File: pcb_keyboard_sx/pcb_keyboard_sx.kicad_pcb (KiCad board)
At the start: 2 copper layers, 172.4 x 135.7 mm, 123 parts, among them SW1 BOOT button, U1 Pico, U2 TRRS

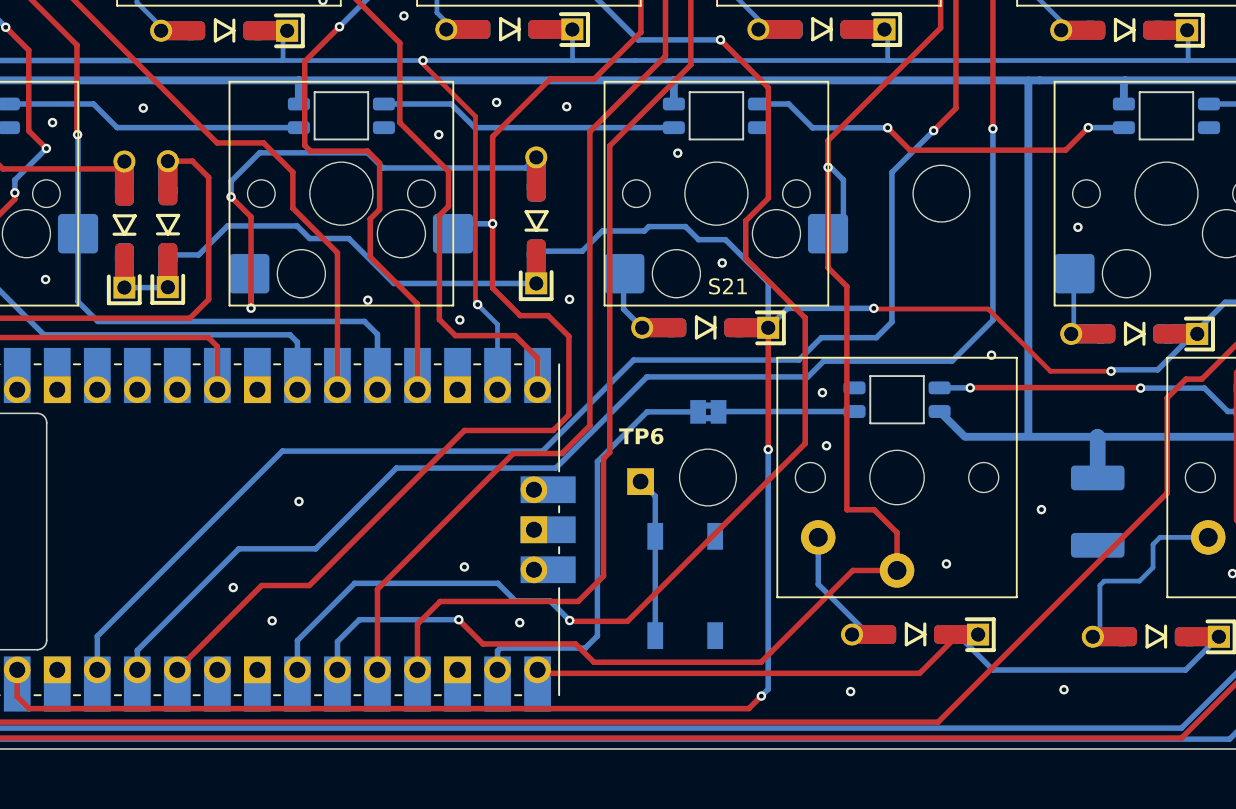
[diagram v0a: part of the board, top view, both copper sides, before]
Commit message: level shifter added also for sx part
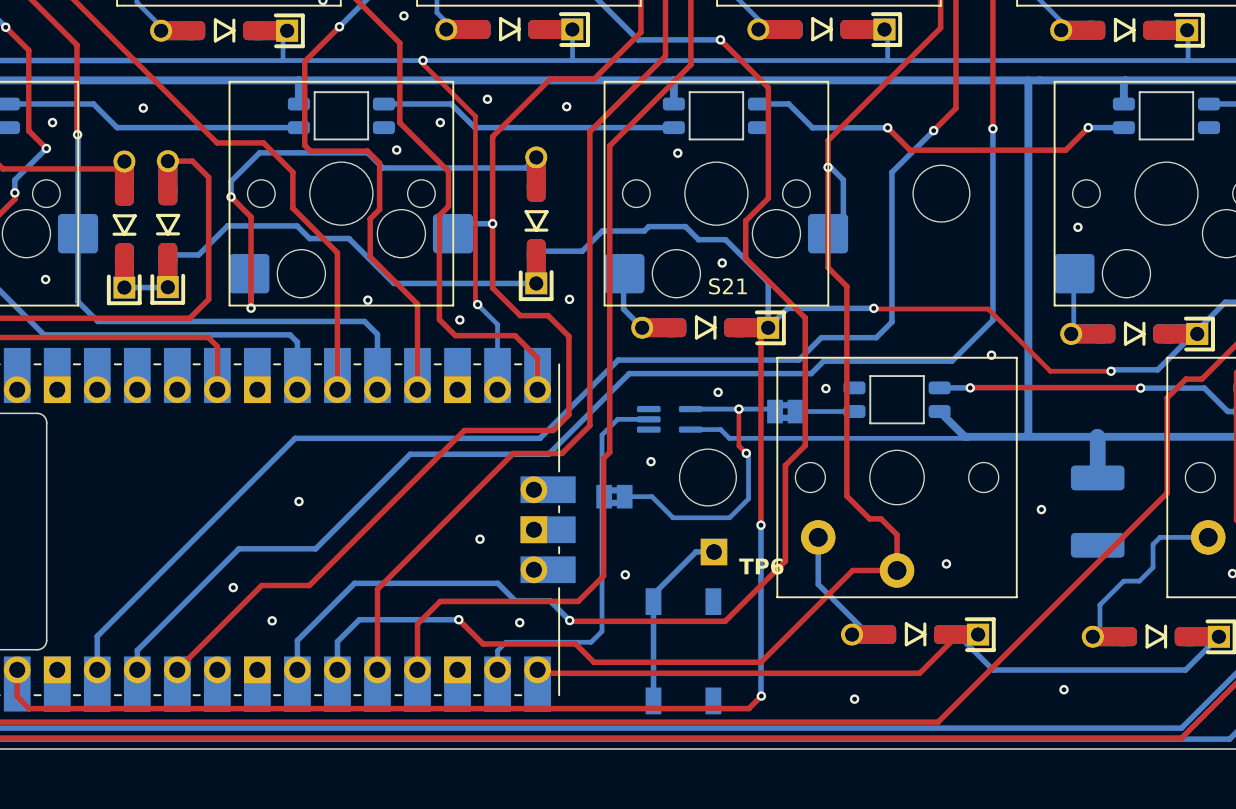
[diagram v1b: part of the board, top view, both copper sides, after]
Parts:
- added JP4: Jumper_2_Bridged, Jumper:SolderJumper-2_P1.3mm_Bridged2Bar_Pad1.0x1.5mm, B.Cu at (98.0, 142.4)
- added U3: 74LVC1G34, Package_TO_SOT_SMD:SOT-353_SC-70-5_Handsoldering, B.Cu at (101.5, 137.5)
- moved TP5 6.46 mm to (104.3, 145.9)
- moved JP3 4.88 mm to (108.9, 137.0)
- moved SW1 4.14 mm to (102.4, 152.2)
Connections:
- JP3 pad 1: LED_GPIO -> LED 5V
- U1 pad 19: LED_GPIO -> LED 3.3V
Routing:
- net LED_GPIO: track 26.7 -> 0.00 mm
- net LED 3.3V: track 0.00 -> 24.2 mm
- net LED 5V: track 0.00 -> 20.3 mm, vias 0 -> 2
- net +5V: track 946.0 -> 964.0 mm
- net Net-(JP3-B): track 8.63 -> 3.75 mm
- net SPLIT_HAND_PIN: track 129.0 -> 132.6 mm
- net Net-(SW1-Pad1): track 10.2 -> 11.3 mm
- net Net-(D29-A): track 12.2 -> 11.4 mm
- net Col 4: track 170.5 -> 169.9 mm
- net GND: vias 131 -> 134
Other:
- board text added: "bypass shifter"

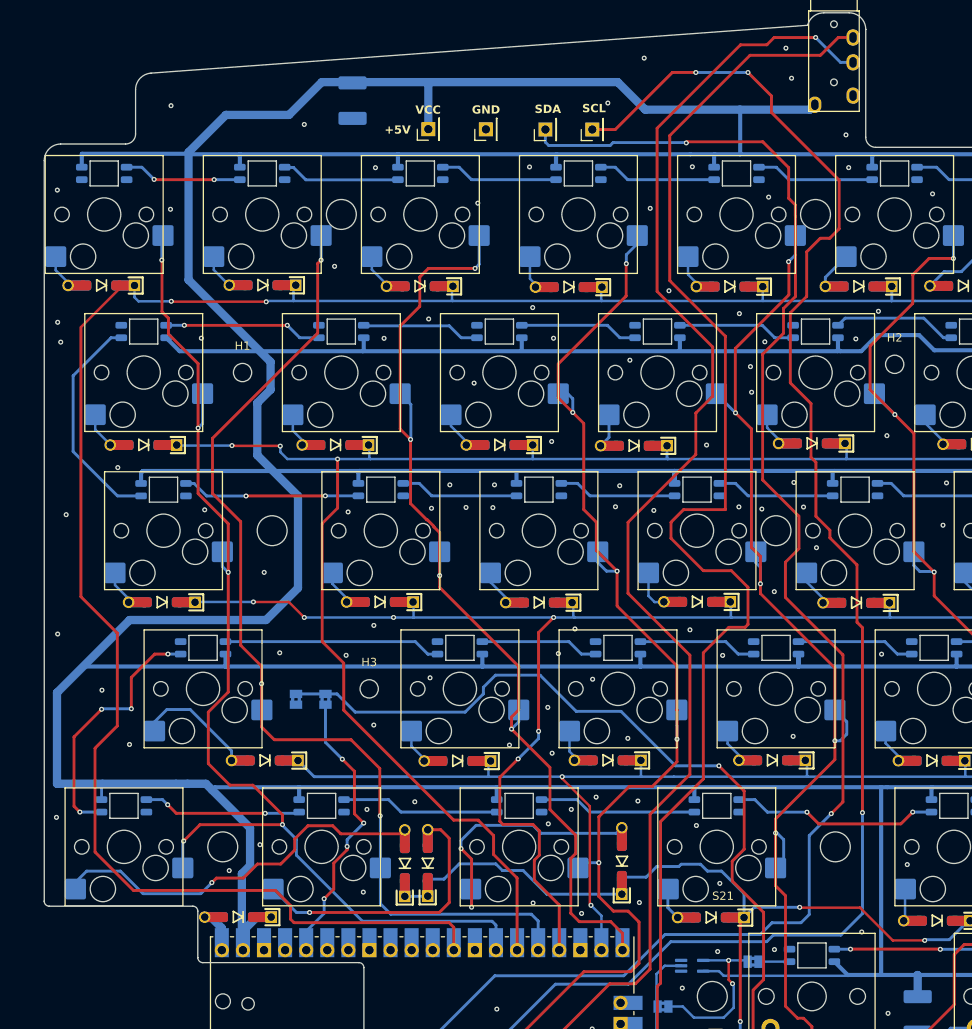
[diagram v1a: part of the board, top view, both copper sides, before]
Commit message: added d+ and d- bus
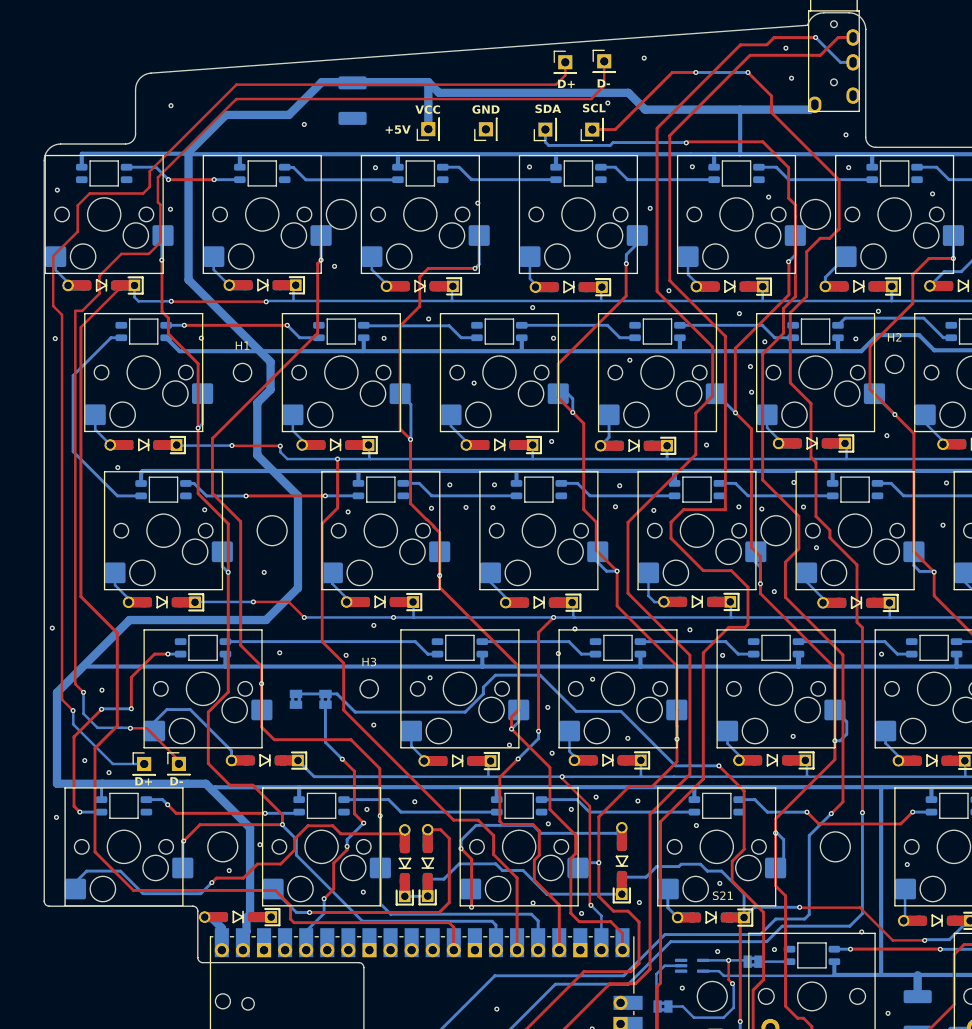
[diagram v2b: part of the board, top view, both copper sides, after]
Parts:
- added TP6: TestPoint, Connector_PinHeader_2.54mm:PinHeader_1x01_P2.54mm_Vertical, F.Cu at (86.2, 28.7)
- added TP7: TestPoint, Connector_PinHeader_2.54mm:PinHeader_1x01_P2.54mm_Vertical, F.Cu at (35.5, 113.2)
- added TP8: TestPoint, Connector_PinHeader_2.54mm:PinHeader_1x01_P2.54mm_Vertical, F.Cu at (90.9, 28.6)
- added TP9: TestPoint, Connector_PinHeader_2.54mm:PinHeader_1x01_P2.54mm_Vertical, F.Cu at (39.7, 113.2)
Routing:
- net Data-: track 0.00 -> 147.3 mm, vias 0 -> 2
- net Data+: track 0.00 -> 143.1 mm, vias 0 -> 1
- net +5V: track 964.0 -> 963.1 mm
- net GND: vias 134 -> 133
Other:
- board text added: "D+"
- board text added: "D-"

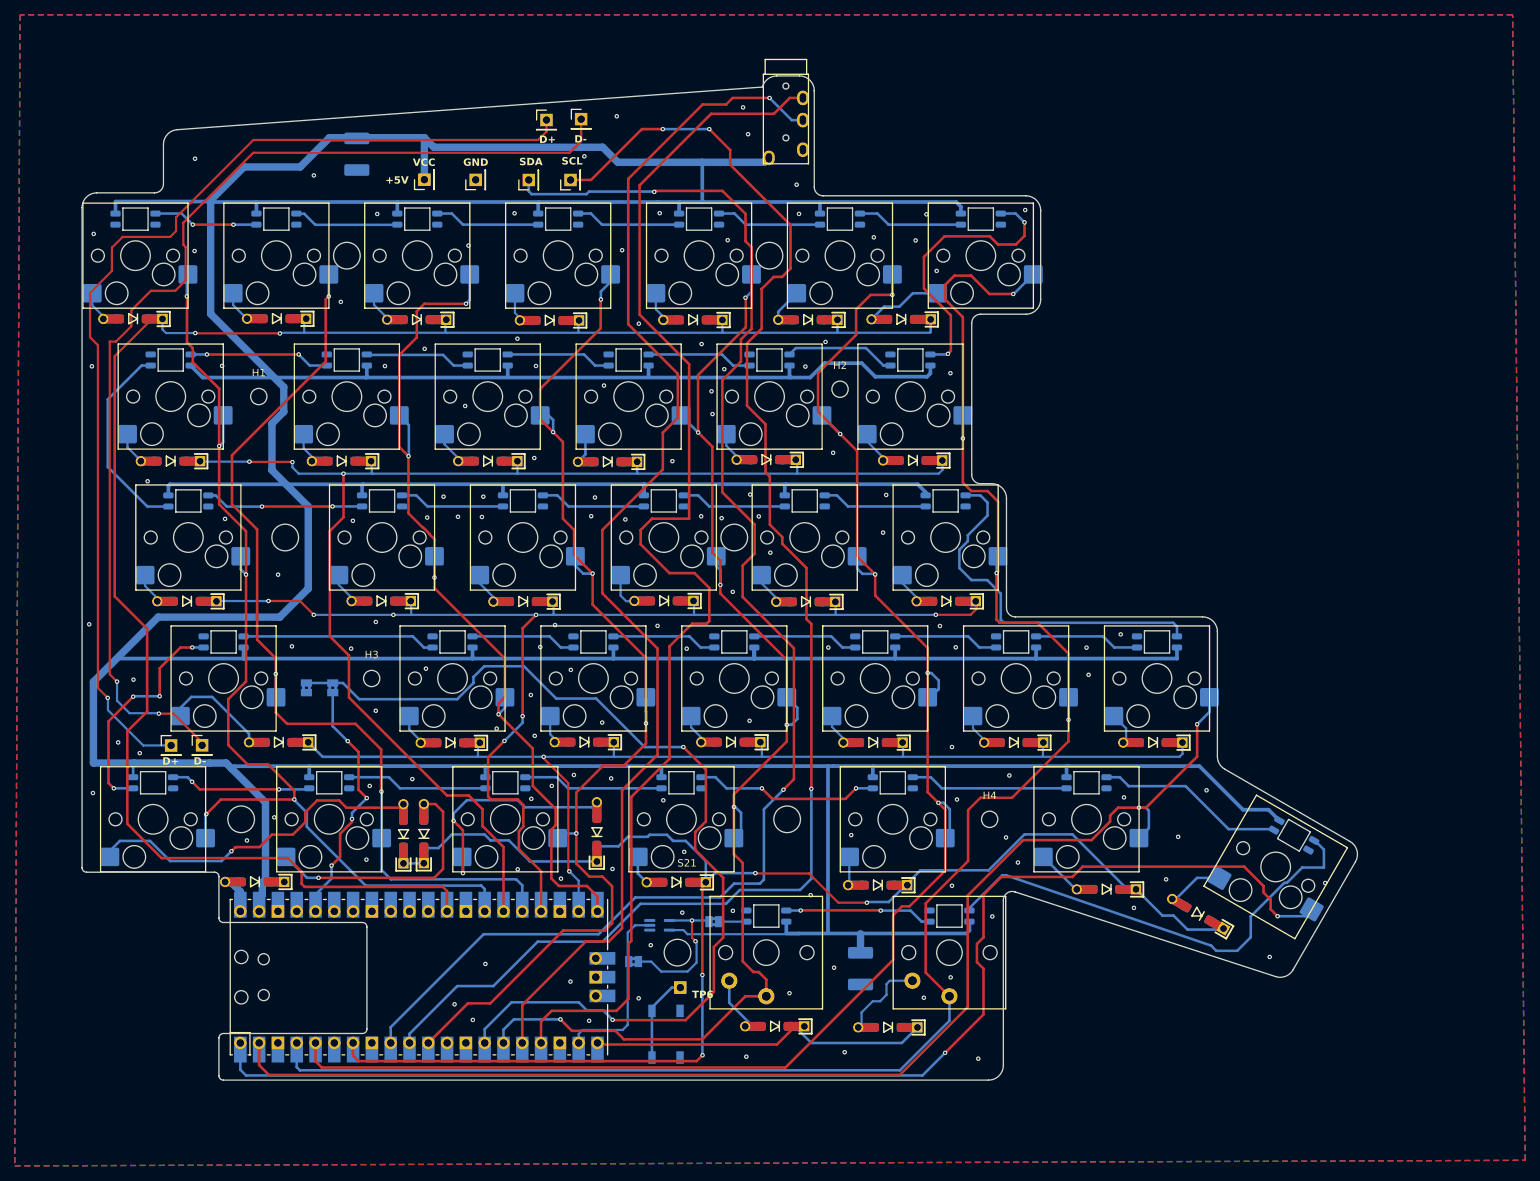
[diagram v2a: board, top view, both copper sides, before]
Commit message: stessi GPIO per dx e sx
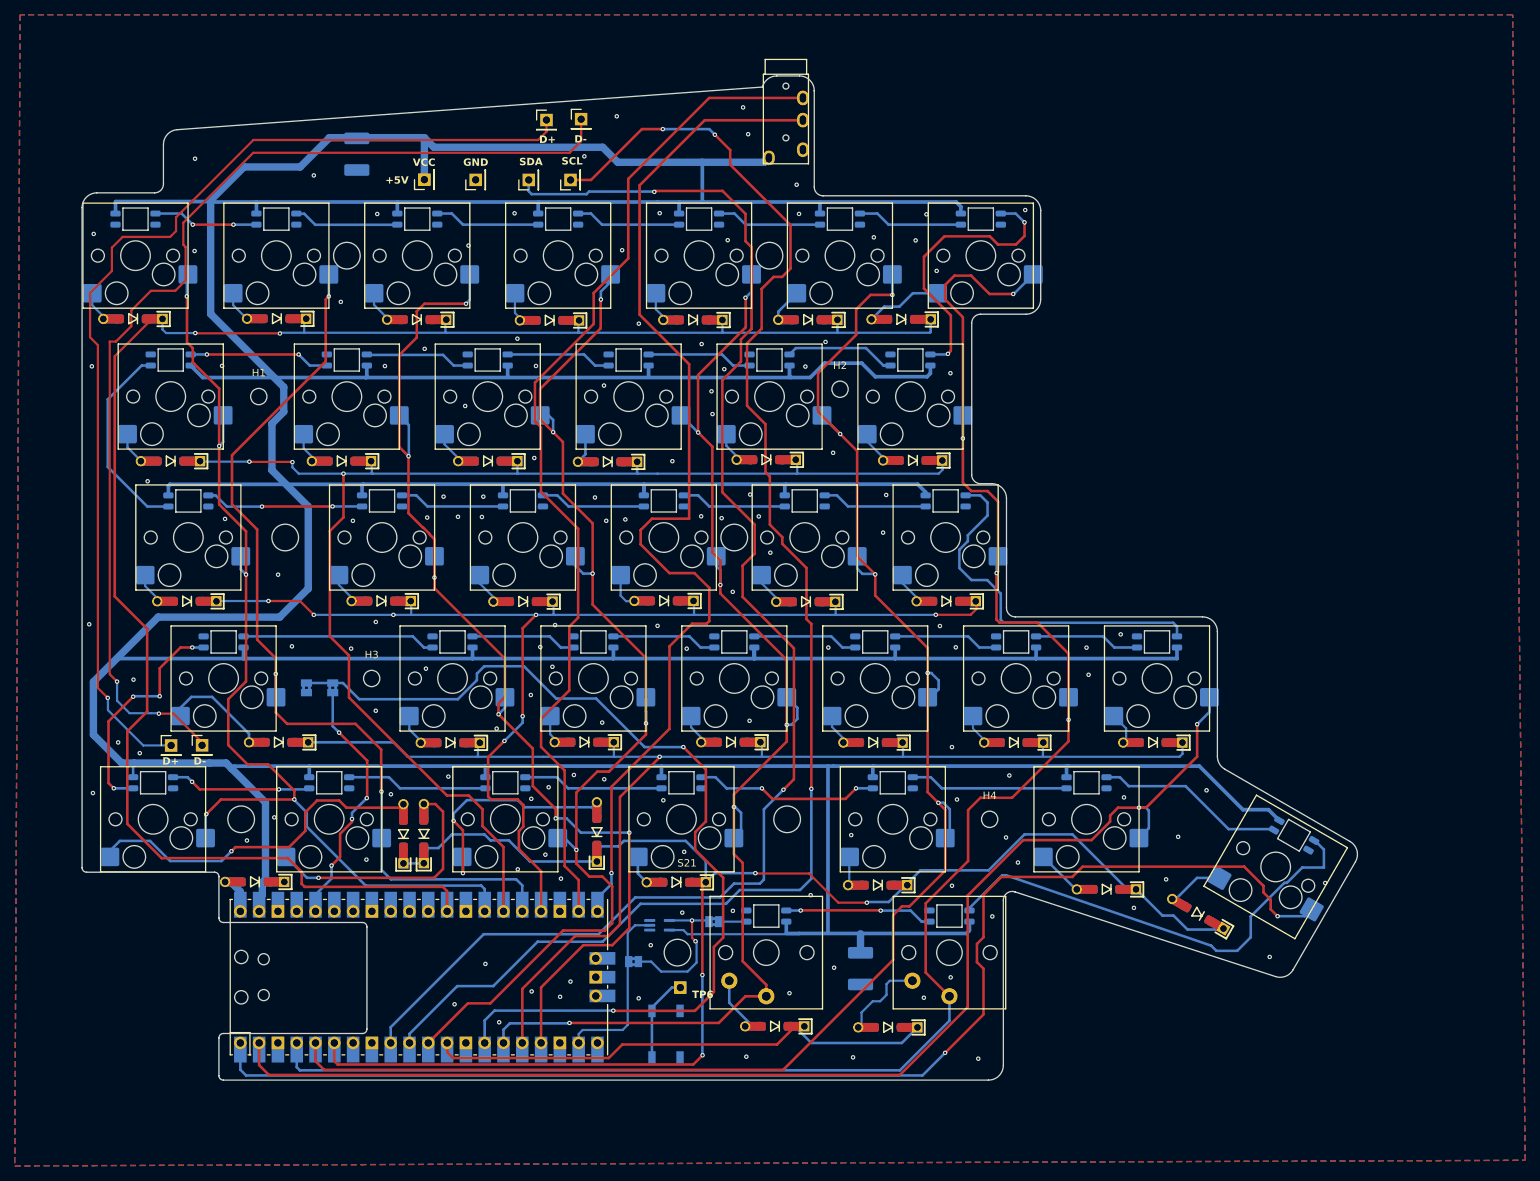
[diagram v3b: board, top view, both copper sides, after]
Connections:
- U1 pad 12: unconnected-(U1-GPIO9-Pad12)_1 -> Row 5
- U1 pad 16: RX -> Row 3
- U1 pad 17: TX -> Col 2
- U1 pad 20: Row 5 -> unconnected-(U1-GPIO15-Pad20)
- U1 pad 21: Col 2 -> RX
- U1 pad 22: Row 3 -> TX
- U1 pad 6: unconnected-(U1-GPIO4-Pad6)_1 -> Row 4
- U1 pad 7: Row 4 -> unconnected-(U1-GPIO5-Pad7)
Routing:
- net TX: track 172.9 -> 138.9 mm
- net Col 2: track 119.5 -> 148.2 mm, vias 4 -> 6
- net Row 3: track 153.9 -> 180.0 mm, vias 2 -> 1
- net Row 5: track 46.2 -> 68.8 mm
- net RX: track 165.6 -> 143.7 mm
- net Row 4: track 202.9 -> 205.5 mm
- net Col 4: track 169.9 -> 167.2 mm
- net +5V: track 963.1 -> 960.7 mm
- net SPLIT_HAND_PIN: track 132.6 -> 131.4 mm
- net Net-(D4-A): track 46.9 -> 47.6 mm
